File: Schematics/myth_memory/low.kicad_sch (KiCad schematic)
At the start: 8 parts, among them U1 74HC04, U10 74LS257, U11 74AHC244, U12 74LS32, U4 74LS32, U7 74AHC273, U8 4075, U9 74LS257

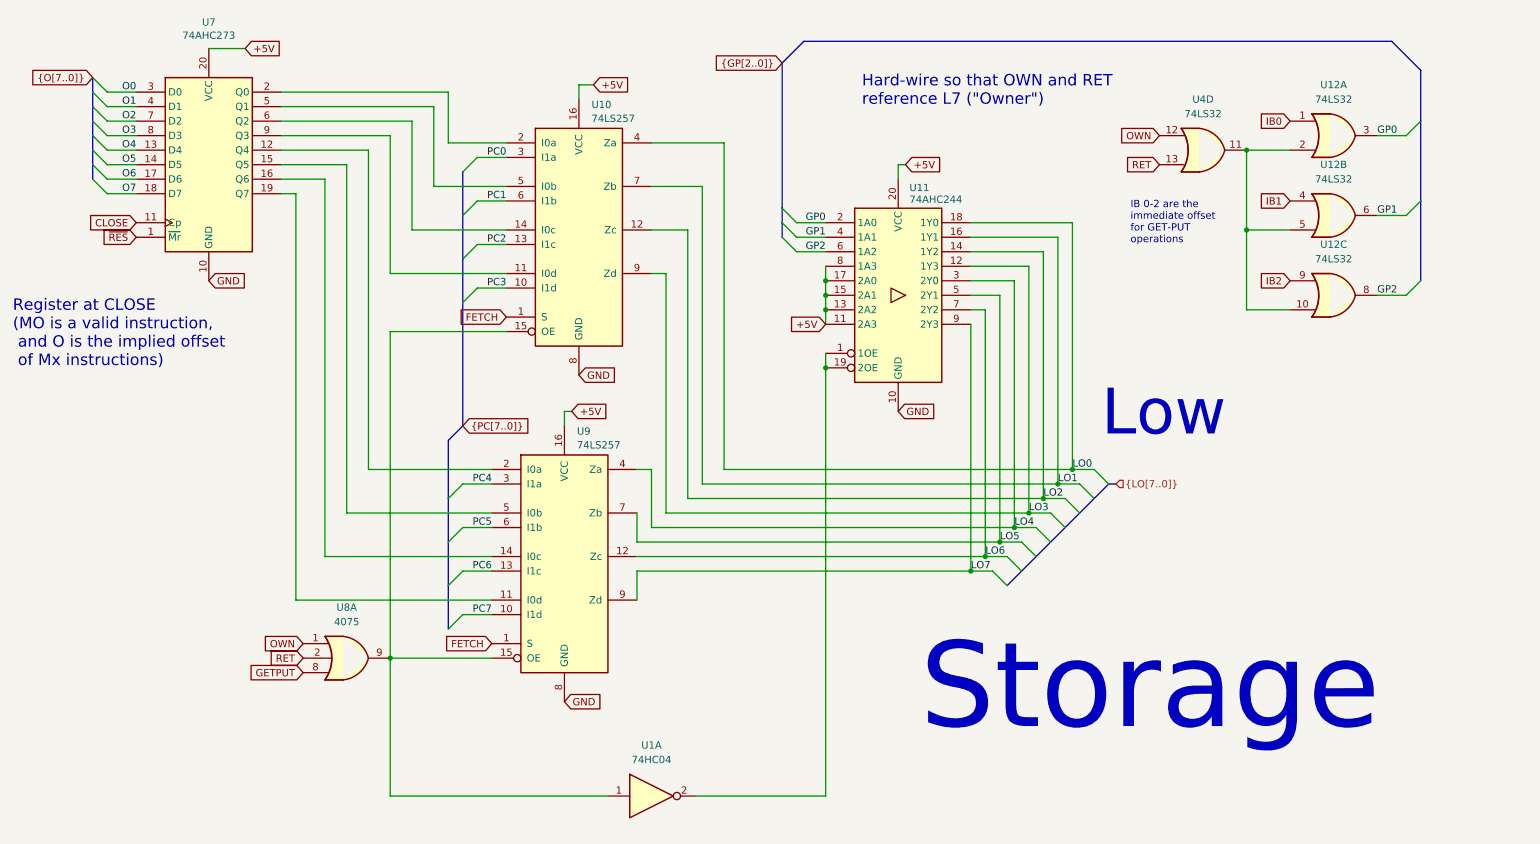
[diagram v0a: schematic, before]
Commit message: Improve schematics for readability
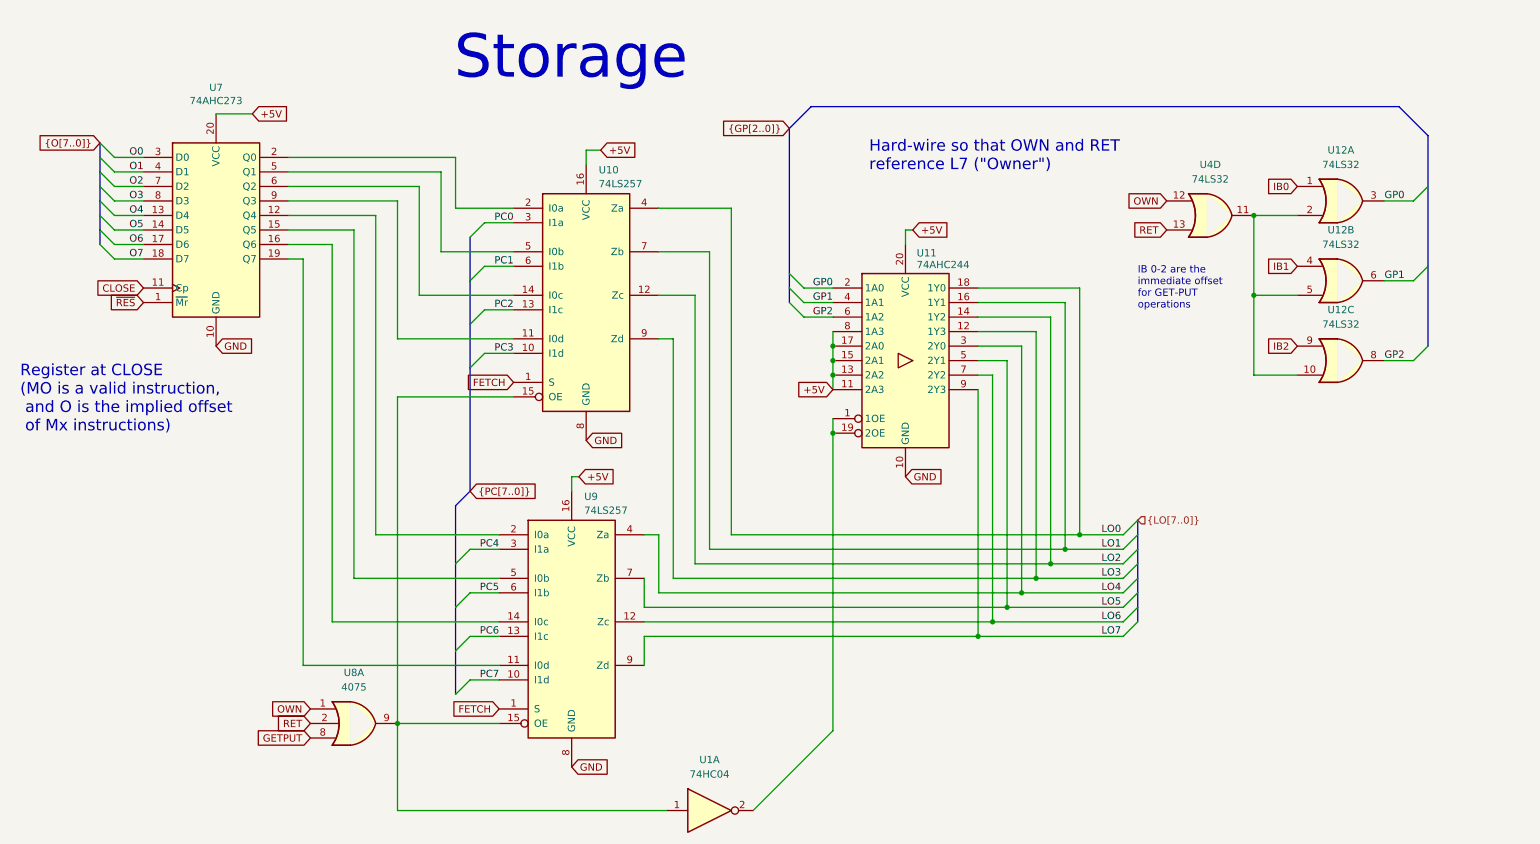
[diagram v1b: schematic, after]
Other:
- note removed: "Low"
- moved on the sheet: U10, U11, U12A, U12B, U12C, U1A, U4D, U7, U8A, U9

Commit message: Change d to g
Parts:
- U1, U12, U4, U8: footprint (none) -> Package_DIP:DIP-14_W7.62mm_LongPads
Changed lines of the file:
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@@
 			)
 		)
-		(property "Footprint" ""
+		(property "Footprint" "Package_DIP:DIP-14_W7.62mm_LongPads"
 			(at 233.68 57.15 0)
 			(effects
@@
 			)
 		)
-		(property "Footprint" ""
+		(property "Footprint" "Package_DIP:DIP-14_W7.62mm_LongPads"
 			(at 256.54 68.58 0)
 			(effects
@@
 			)
 		)
-		(property "Footprint" ""
+		(property "Footprint" "Package_DIP:DIP-14_W7.62mm_LongPads"
 			(at 83.82 146.05 0)
 			(effects
@@
 			)
 		)
-		(property "Footprint" ""
+		(property "Footprint" "Package_DIP:DIP-14_W7.62mm_LongPads"
 			(at 256.54 82.55 0)
 			(effects
@@
 			)
 		)
-		(property "Footprint" ""
+		(property "Footprint" "Package_DIP:DIP-14_W7.62mm_LongPads"
 			(at 256.54 54.61 0)
 			(effects
@@
 			)
 		)
-		(property "Footprint" ""
+		(property "Footprint" "Package_DIP:DIP-14_W7.62mm_LongPads"
 			(at 146.05 161.29 0)
 			(effects
